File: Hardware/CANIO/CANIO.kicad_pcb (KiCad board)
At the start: 2 copper layers, 11 parts, among them J201 CAN, J202 CAN, U201 MCP25625-x-SS, Y201 16mHz

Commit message: Add processor
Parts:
- added C101: 1u, Capacitor_SMD:C_0805_2012Metric, F.Cu at (31.6, 9.58)
- added C102: 100nF, Capacitor_SMD:C_0805_2012Metric, F.Cu at (31.6, 12.6)
- added C103: 10uf, Capacitor_SMD:CP_Elec_4x3, F.Cu at (37.8, 11.0)
- added C104: 100nF, Capacitor_SMD:C_0805_2012Metric, F.Cu at (31.6, 15.6)
- added C105: 1uF, Capacitor_SMD:C_0805_2012Metric, F.Cu at (31.6, 18.6)
- added D101: MBR0520LT, Diode_SMD:D_SOD-123, F.Cu at (22.5, 18.0)
- added D102: STAT, LED_SMD:LED_0805_2012Metric, F.Cu at (36.1, 15.4)
- added D103: PWR, LED_SMD:LED_0805_2012Metric, F.Cu at (36.1, 18.5)
- added J101: USBC, KenwoodFox:USB_C_Receptacle_XKB_U262-16XN-4BVC11_Full_Pads, F.Cu at (49.7, 4.78)
- added J102: Tag Connect, Connector:Tag-Connect_TC2050-IDC-FP_2x05_P1.27mm_Vertical, F.Cu at (37.2, 1.20)
- added R101: 22R, Resistor_SMD:R_0805_2012Metric, F.Cu at (17.4, -2.10)
- added R102: 22R, Resistor_SMD:R_0805_2012Metric, F.Cu at (17.4, 0.85)
- added R103: 10k, Resistor_SMD:R_0805_2012Metric, F.Cu at (17.4, 3.80)
- added R104: 5K1, Resistor_SMD:R_0805_2012Metric, F.Cu at (17.4, 6.75)
- added R105: 5K1, Resistor_SMD:R_0805_2012Metric, F.Cu at (17.4, 9.70)
- added R106: 1K, Resistor_SMD:R_0805_2012Metric, F.Cu at (17.4, 12.7)
- added R107: 1K, Resistor_SMD:R_0805_2012Metric, F.Cu at (17.4, 15.6)
- added U101: ATmega16U2, Package_QFP:TQFP-32_7x7mm_P0.8mm, F.Cu at (25.4, 2.25)
- added U102: LM1117MP-5.0, Package_TO_SOT_SMD:SOT-223-3_TabPin2, F.Cu at (24.5, 12.2)
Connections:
- net Net-(U201-STBY) renamed /CANBUS/STBY
- U201 pad 13: unconnected-(U201-~{INT}-Pad13) -> /CANBUS/INT
- U201 pad 22: /CANBUS/CLKOUT -> /CLKOUT

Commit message: Bump
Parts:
- moved J101 43.7 mm to (34.0, -36.0)
- moved C203 28.8 mm to (25.9, 22.0)
- moved R202 28.8 mm to (25.9, 25.0)
- moved C102 22.8 mm to (35.3, 35.1)
- moved D102 22.8 mm to (39.8, 37.9)
- moved D103 22.8 mm to (39.8, 41.0)
- moved R105 22.8 mm to (21.0, 32.2)
- moved U102 22.8 mm to (28.1, 34.7)
- moved C101 22.8 mm to (35.3, 32.1)
- moved C103 22.8 mm to (41.4, 33.5)
- moved C104 22.8 mm to (35.3, 38.1)
- moved C105 22.8 mm to (35.3, 41.1)
- moved D101 22.8 mm to (26.1, 40.5)
- moved R101 22.8 mm to (21.0, 20.4)
- moved R102 22.8 mm to (21.0, 23.4)
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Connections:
- U201 pad 14: /CANBUS/SCK -> /ICSP_SCK
- U201 pad 15: /CANBUS/SI -> /ICSP_MOSI
- U201 pad 16: /CANBUS/SO -> /ICSP_MISO

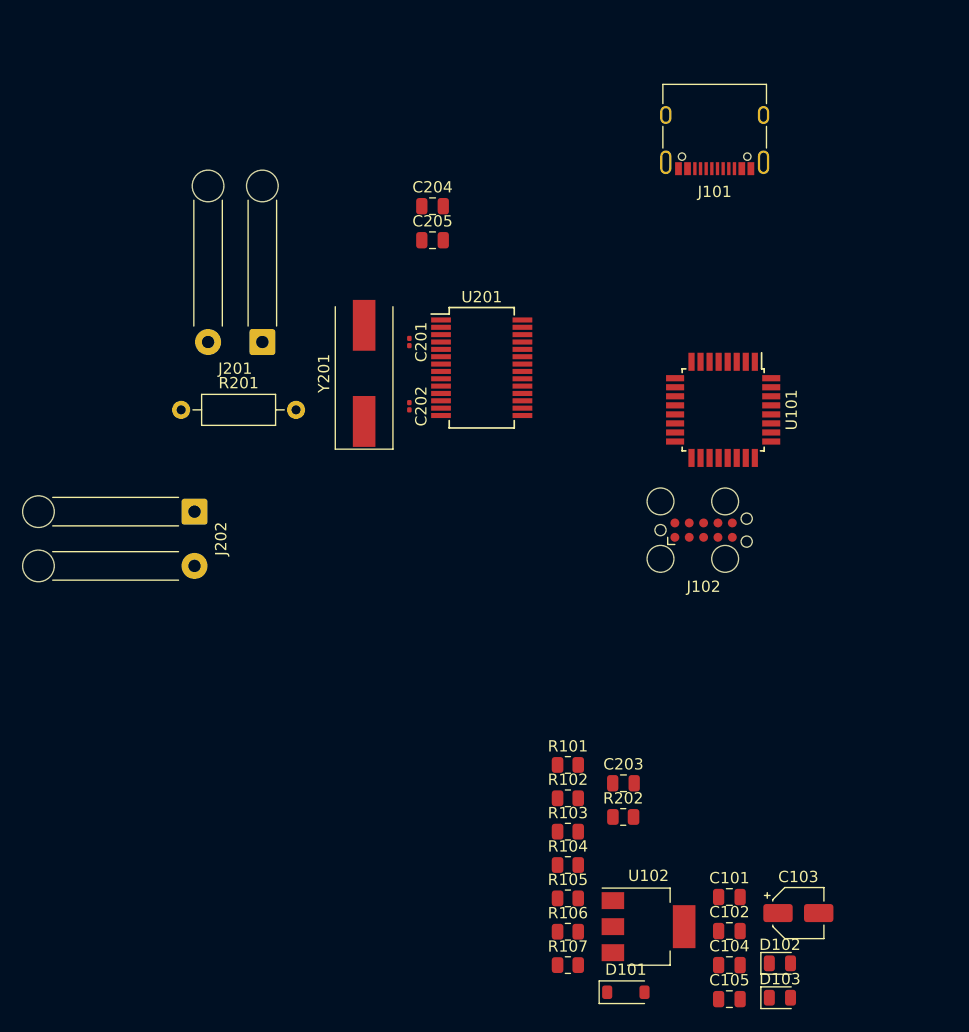
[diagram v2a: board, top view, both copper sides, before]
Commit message: Edge cuts and stuff
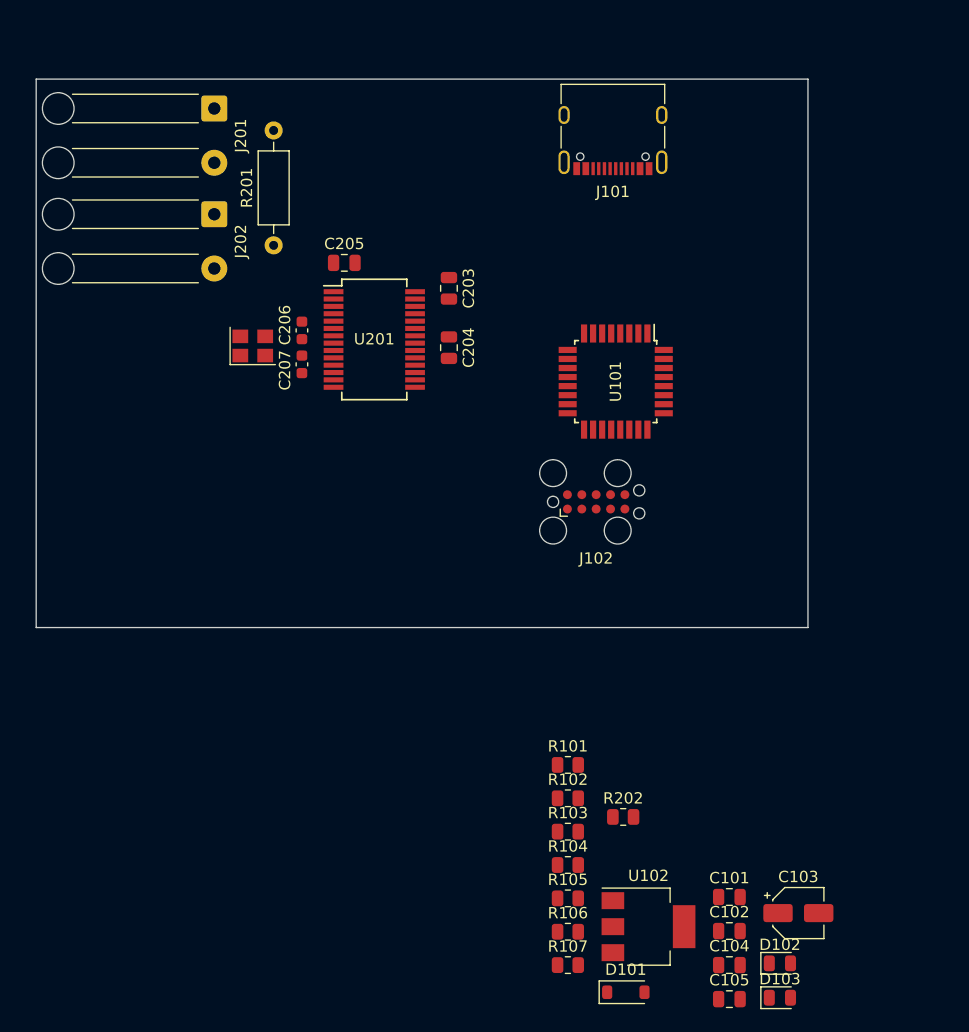
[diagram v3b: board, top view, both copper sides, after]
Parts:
- removed C201, C202: 22pf, Capacitor_SMD:C_0201_0603Metric
- removed Y201: 16mHz, Crystal:Crystal_SMD_HC49-SD
- added C206: 22pf, Capacitor_SMD:C_0603_1608Metric, F.Cu at (-2.50, -18.0)
- added C207: 22pf, Capacitor_SMD:C_0603_1608Metric, F.Cu at (-2.50, -15.0)
- added Y202: Crystal_GND24, Crystal:Crystal_SMD_3225-4Pin_3.2x2.5mm, F.Cu at (-6.85, -16.6)
- moved C203 46.4 mm to (10.5, -21.8), turned to 90 degrees
- moved J202 26.4 mm to (-10.2, -28.3)
- moved J201 21.1 mm to (-10.2, -37.6), turned to -90 degrees
- moved R201 16.7 mm to (-5.00, -25.6), turned to 90 degrees
- moved C204 12.6 mm to (10.5, -16.5), turned to 90 degrees
- moved J102 9.82 mm to (23.5, -2.87)
- moved U101 9.82 mm to (25.2, -13.5)
- moved U201 9.82 mm to (3.90, -17.2)
- moved J101 9.00 mm to (25.0, -36.0)
- moved C205 8.05 mm to (1.25, -24.0)
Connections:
- U201 pad 8: Net-(U201-OSC2) -> /CANBUS/XTAL2
- U201 pad 9: Net-(U201-OSC1) -> /CANBUS/XTAL1
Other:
- board outline added: 68.2 x 48.5 mm

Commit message: Fix ERC
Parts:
- removed J101: USBC, KenwoodFox:USB_C_Receptacle_XKB_U262-16XN-4BVC11_Full_Pads
- added J103: PWR, Connector_JST:JST_XH_S2B-XH-A_1x02_P2.50mm_Horizontal, F.Cu at (-20.5, -1.50)
- added P101: USB_C_Plug_USB2.0, KenwoodFox:USB_C_Receptacle_XKB_U262-16XN-4BVC11_Full_Pads, F.Cu at (29.8, -36.1)

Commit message: Arthur is encouraging
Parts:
- removed C103: 10uf, Capacitor_SMD:CP_Elec_4x3
- removed C104: 100nF, Capacitor_SMD:C_0805_2012Metric
- removed C105: 1uF, Capacitor_SMD:C_0805_2012Metric
- removed D103: PWR, LED_SMD:LED_0805_2012Metric
- removed R107: 1K, Resistor_SMD:R_0805_2012Metric
- removed U102: LM1117MP-5.0, Package_TO_SOT_SMD:SOT-223-3_TabPin2
- moved D101 70.9 mm to (35.6, -29.8), turned to 180 degrees
- moved R105 68.6 mm to (37.0, -34.5), turned to 90 degrees
- moved D102 66.0 mm to (22.2, -25.7), turned to 90 degrees
- moved R104 63.8 mm to (22.5, -34.5), turned to 90 degrees
- moved R106 57.2 mm to (22.2, -22.0), turned to 90 degrees
- moved R102 52.2 mm to (28.8, -28.2), turned to -90 degrees
- moved C102 51.4 mm to (32.5, -16.2)
- moved R101 49.6 mm to (30.8, -28.2), turned to -90 degrees
- moved C101 44.4 mm to (32.5, -12.2)
- moved R202 43.5 mm to (0.00, -10.0)
- moved R103 34.2 mm to (30.8, -6.50)
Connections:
- J103 pad 2: +12V -> +5V
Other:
- board text added: "CANH"
- board text added: "CANL"

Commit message: Always have a backup
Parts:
- added C103: DNP, Capacitor_SMD:C_0603_1608Metric, F.Cu at (35.0, -22.7)
- added C104: DNP, Capacitor_SMD:C_0603_1608Metric, F.Cu at (35.0, -19.5)
- added JP101: SolderJumper_2_Bridged, Jumper:SolderJumper-2_P1.3mm_Bridged2Bar_Pad1.0x1.5mm, B.Cu at (16.5, -19.1)
- added Y101: DNP, Crystal:Crystal_SMD_3225-4Pin_3.2x2.5mm, F.Cu at (38.0, -21.2)
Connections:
- U101 pad 1: /CLKOUT -> /XTAL1
- U101 pad 2: unconnected-(U101-PC0/XTAL2-Pad2) -> /XTAL2

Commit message: My favorite switch
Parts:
- added R107: 10K, Resistor_SMD:R_0805_2012Metric, F.Cu at (16.0, -9.00)
- added SW101: RESET, Button_Switch_THT:SW_PUSH_6mm_H4.3mm, F.Cu at (38.0, 3.00)
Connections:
- U101 pad 13: unconnected-(U101-~{HWB}/PD7-Pad13) -> Net-(U101-~{HWB}/PD7)
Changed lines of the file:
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@@
   (net 40 "unconnected-(U101-PD5-Pad11)")
   (net 41 "unconnected-(U101-PD6-Pad12)")
-  (net 42 "unconnected-(U101-~{HWB}{slash}PD7-Pad13)")
+  (net 42 "Net-(U101-~{HWB}{slash}PD7)")
   (net 43 "unconnected-(U101-PB0-Pad14)")
   (net 44 "unconnected-(U101-PB4-Pad18)")
@@
       (net 41 "unconnected-(U101-PD6-Pad12)") (pinfunction "PD6") (pintype "bidirectional+no_connect"))
     (pad "13" smd rect (at 0.4 4.25) (size 1.6 0.55) (layers "F.Cu" "F.Paste" "F.Mask")
-      (net 42 "unconnected-(U101-~{HWB}{slash}PD7-Pad13)") (pinfunction "~{HWB}/PD7") (pintype "bidirectional+no_connect"))
+      (net 42 "Net-(U101-~{HWB}{slash}PD7)") (pinfunction "~{HWB}/PD7") (pintype "bidirectional"))
     (pad "14" smd rect (at 1.2 4.25) (size 1.6 0.55) (layers "F.Cu" "F.Paste" "F.Mask")
       (net 43 "unconnected-(U101-PB0-Pad14)") (pinfunction "PB0") (pintype "bidirectional+no_connect"))
@@
   )
   (footprint "Resistor_SMD:R_0805_2012Metric" (layer "F.Cu")
+    (at 16 -9 90)
+    (descr "Resistor SMD 0805 (2012 Metric), square (rectangular) end terminal, IPC_7351 nominal, (Body size source: IPC-SM-782 page 72, https://www.pcb-3d.com/wordpress/wp-content/uploads/ipc-sm-782a_amendment_1_and_2.pdf), generated with kicad-footprint-generator")
+    (tags "resistor")
+    (property "LCSC#" "C269748")
+    (property "Sheetfile" "CANIO.kicad_sch")
+    (property "Sheetname" "")
+    (property "ki_description" "Resistor, small symbol")
+    (property "ki_keywords" "R resistor")
+    (attr smd)
+    (fp_text reference "R107" (at 0 -1.65 90) (layer "F.SilkS")
+        (effects (font (size 1 1) (thickness 0.15)))
+    )
+    (fp_text value "10K" (at 0 1.65 90) (layer "F.Fab")
+        (effects (font (size 1 1) (thickness 0.15)))
+    )
+    (fp_text user "${REFERENCE}" (at 0 0 90) (layer "F.Fab")
+        (effects (font (size 0.5 0.5) (thickness 0.08)))
+    )
+    (fp_line (start -0.227064 -0.735) (end 0.227064 -0.735)
+      (stroke (width 0.12) (type solid)) (layer "F.SilkS"))
+    (fp_line (start -0.227064 0.735) (end 0.227064 0.735)
+      (stroke (width 0.12) (type solid)) (layer "F.SilkS"))
+    (fp_line (start -1.68 -0.95) (end 1.68 -0.95)
+      (stroke (width 0.05) (type solid)) (layer "F.CrtYd"))
+    (fp_line (start -1.68 0.95) (end -1.68 -0.95)
+      (stroke (width 0.05) (type solid)) (layer "F.CrtYd"))
+    (fp_line (start 1.68 -0.95) (end 1.68 0.95)
+      (stroke (width 0.05) (type solid)) (layer "F.CrtYd"))
+    (fp_line (start 1.68 0.95) (end -1.68 0.95)
+      (stroke (width 0.05) (type solid)) (layer "F.CrtYd"))
+    (fp_line (start -1 -0.625) (end 1 -0.625)
+      (stroke (width 0.1) (type solid)) (layer "F.Fab"))
+    (fp_line (start -1 0.625) (end -1 -0.625)
+      (stroke (width 0.1) (type solid)) (layer "F.Fab"))
+    (fp_line (start 1 -0.625) (end 1 0.625)
+      (stroke (width 0.1) (type solid)) (layer "F.Fab"))
+    (fp_line (start 1 0.625) (end -1 0.625)
+      (stroke (width 0.1) (type solid)) (layer "F.Fab"))
+    (pad "1" smd roundrect (at -0.9125 0 90) (size 1.025 1.4) (layers "F.Cu" "F.Paste" "F.Mask") (roundrect_rratio 0.243902)
+      (net 1 "GND") (pintype "passive"))
+    (pad "2" smd roundrect (at 0.9125 0 90) (size 1.025 1.4) (layers "F.Cu" "F.Paste" "F.Mask") (roundrect_rratio 0.243902)
+      (net 42 "Net-(U101-~{HWB}{slash}PD7)") (pintype "passive"))
+    (model "${KICAD6_3DMODEL_DIR}/Resistor_SMD.3dshapes/R_0805_2012Metric.wrl"
+      (offset (xyz 0 0 0))
+      (scale (xyz 1 1 1))
+      (rotate (xyz 0 0 0))
+    )
+  )
+  (footprint "Resistor_SMD:R_0805_2012Metric" (layer "F.Cu")
     (at 28.75 -28.25 -90)
     (descr "Resistor SMD 0805 (2012 Metric), square (rectangular) end terminal, IPC_7351 nominal, (Body size source: IPC-SM-782 page 72, https://www.pcb-3d.com/wordpress/wp-content/uploads/ipc-sm-782a_amendment_1_and_2.pdf), generated with kicad-footprint-generator")
@@
       (offset (xyz 0 0 0))
       (scale (xyz 1 1 1))
+      (rotate (xyz 0 0 0))
+    )
+  )
+  (footprint "Button_Switch_THT:SW_PUSH_6mm_H4.3mm" (layer "F.Cu")
+    (at 38 3 180)
+    (descr "tactile push button, 6x6mm e.g. PHAP33xx series, height=4.3mm")
+    (tags "tact sw push 6mm")
+    (property "Sheetfile" "CANIO.kicad_sch")
+    (property "Sheetname" "")
+    (property "ki_description" "Push button switch, generic, two pins")
+    (property "ki_keywords" "switch normally-open pushbutton push-button")
+    (attr through_hole)
+    (fp_text reference "SW101" (at 3.25 -2) (layer "F.SilkS") hide
+        (effects (font (size 1 1) (thickness 0.15)))
+    )
+    (fp_text value "RESET" (at 3 -2.5) (layer "F.SilkS")
+        (effects (font (size 1 1) (thickness 0.15)))
+    )
+    (fp_text user "${REFERENCE}" (at 3.25 2.25) (layer "F.Fab")
+        (effects (font (size 1 1) (thickness 0.15)))
+    )
+    (fp_line (start -0.25 1.5) (end -0.25 3)
+      (stroke (width 0.12) (type solid)) (layer "F.SilkS"))
+    (fp_line (start 1 5.5) (end 5.5 5.5)
+      (stroke (width 0.12) (type solid)) (layer "F.SilkS"))
+    (fp_line (start 5.5 -1) (end 1 -1)
+      (stroke (width 0.12) (type solid)) (layer "F.SilkS"))
+    (fp_line (start 6.75 3) (end 6.75 1.5)
+      (stroke (width 0.12) (type solid)) (layer "F.SilkS"))
+    (fp_line (start -1.5 -1.5) (end -1.25 -1.5)
+      (stroke (width 0.05) (type solid)) (layer "F.CrtYd"))
+    (fp_line (start -1.5 -1.25) (end -1.5 -1.5)
+      (stroke (width 0.05) (type solid)) (layer "F.CrtYd"))
+    (fp_line (start -1.5 5.75) (end -1.5 -1.25)
+      (stroke (width 0.05) (type solid)) (layer "F.CrtYd"))
+    (fp_line (start -1.5 5.75) (end -1.5 6)
+      (stroke (width 0.05) (type solid)) (layer "F.CrtYd"))
+    (fp_line (start -1.5 6) (end -1.25 6)
+      (stroke (width 0.05) (type solid)) (layer "F.CrtYd"))
+    (fp_line (start -1.25 -1.5) (end 7.75 -1.5)
+      (stroke (width 0.05) (type solid)) (layer "F.CrtYd"))
+    (fp_line (start 7.75 -1.5) (end 8 -1.5)
+      (stroke (width 0.05) (type solid)) (layer "F.CrtYd"))
+    (fp_line (start 7.75 6) (end -1.25 6)
+      (stroke (width 0.05) (type solid)) (layer "F.CrtYd"))
+    (fp_line (start 7.75 6) (end 8 6)
+      (stroke (width 0.05) (type solid)) (layer "F.CrtYd"))
+    (fp_line (start 8 -1.5) (end 8 -1.25)
+      (stroke (width 0.05) (type solid)) (layer "F.CrtYd"))
+    (fp_line (start 8 -1.25) (end 8 5.75)
+      (stroke (width 0.05) (type solid)) (layer "F.CrtYd"))
+    (fp_line (start 8 6) (end 8 5.75)
+      (stroke (width 0.05) (type solid)) (layer "F.CrtYd"))
+    (fp_line (start 0.25 -0.75) (end 3.25 -0.75)
+      (stroke (width 0.1) (type solid)) (layer "F.Fab"))
+    (fp_line (start 0.25 5.25) (end 0.25 -0.75)
+      (stroke (width 0.1) (type solid)) (layer "F.Fab"))
+    (fp_line (start 3.25 -0.75) (end 6.25 -0.75)
+      (stroke (width 0.1) (type solid)) (layer "F.Fab"))
+    (fp_line (start 6.25 -0.75) (end 6.25 5.25)
+      (stroke (width 0.1) (type solid)) (layer "F.Fab"))
+    (fp_line (start 6.25 5.25) (end 0.25 5.25)
+      (stroke (width 0.1) (type solid)) (layer "F.Fab"))
+    (fp_circle (center 3.25 2.25) (end 1.25 2.5)
+      (stroke (width 0.1) (type solid)) (fill none) (layer "F.Fab"))
+    (pad "1" thru_hole circle (at 0 0 270) (size 2 2) (drill 1.1) (layers "*.Cu" "*.Mask")
+      (net 22 "/ICSP_RST") (pinfunction "1") (pintype "passive"))
+    (pad "1" thru_hole circle (at 6.5 0 270) (size 2 2) (drill 1.1) (layers "*.Cu" "*.Mask")
+      (net 22 "/ICSP_RST") (pinfunction "1") (pintype "passive"))
+    (pad "2" thru_hole circle (at 0 4.5 270) (size 2 2) (drill 1.1) (layers "*.Cu" "*.Mask")
+      (net 1 "GND") (pinfunction "2") (pintype "passive"))
+    (pad "2" thru_hole circle (at 6.5 4.5 270) (size 2 2) (drill 1.1) (layers "*.Cu" "*.Mask")
+      (net 1 "GND") (pinfunction "2") (pintype "passive"))
+    (model "${KICAD6_3DMODEL_DIR}/Button_Switch_THT.3dshapes/SW_PUSH_6mm_H4.3mm.wrl"
+      (offset (xyz 0 0 0))
+      (scale (xyz 1 1 1))
